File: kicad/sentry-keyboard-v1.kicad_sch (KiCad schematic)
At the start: 269 parts, among them J2 Conn_01x04, J4 AVR-ISP-6, SW1 Reset, SW2 RotaryEncoder_Switch, U1 ATmega32U4-AU, Y1 16Mhz

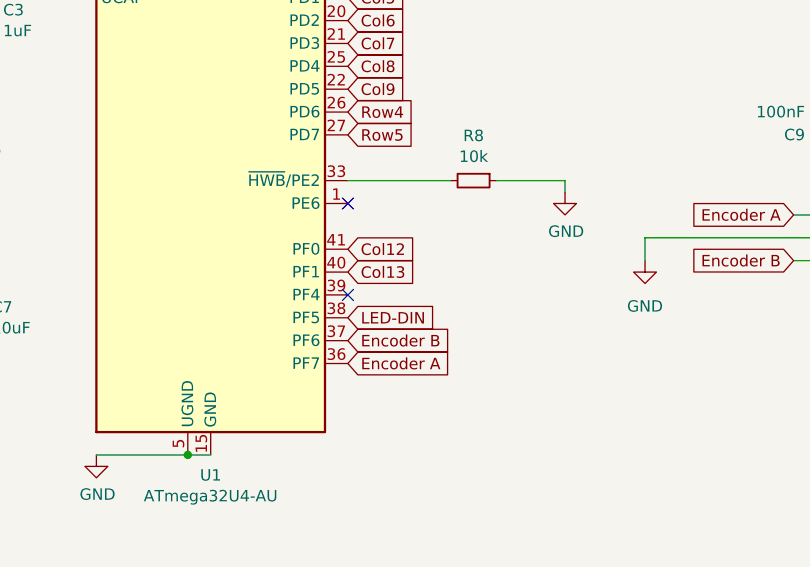
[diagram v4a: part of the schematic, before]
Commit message: Route col 12 and 13
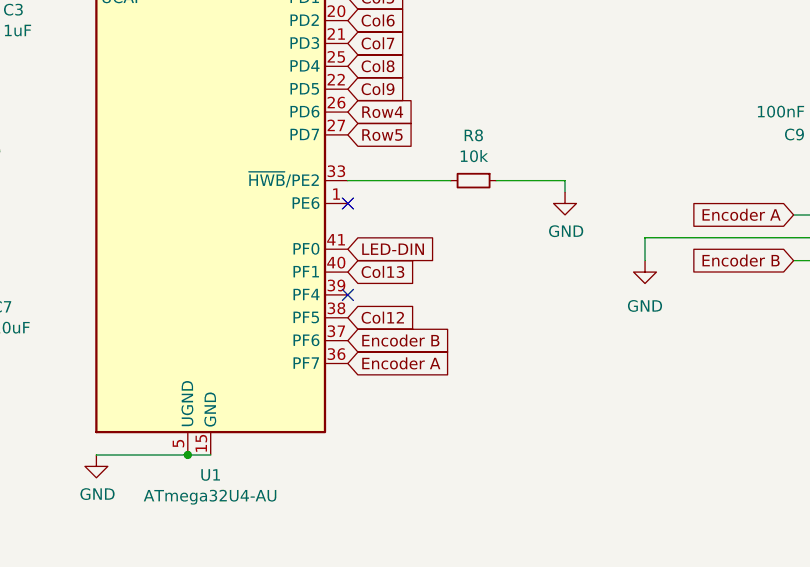
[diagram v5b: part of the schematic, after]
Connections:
- net Col12: now also U1.38 (PF5); no longer U1.41 (PF0)
- net LED-DIN: now also U1.41 (PF0); no longer U1.38 (PF5)
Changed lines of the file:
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@@
+		)
+	)
+	(global_label "LED-DIN"
+		(shape input)
+		(at 96.52 110.49 0)
+		(fields_autoplaced yes)
+		(effects
+			(font
+				(size 1.27 1.27)
+			)
+			(justify left)
+		)
+		(property "Intersheetrefs" "${INTERSHEET_REFS}"
+			(at 107.73 110.49 0)
+			(effects
+				(font
+					(size 1.27 1.27)
+				)
+				(justify left)
+				(hide yes)
+			)
 		)
 	)
@@
 		)
 	)
+	(global_label "Col12"
+		(shape input)
+		(at 96.52 118.11 0)
+		(fields_autoplaced yes)
+		(effects
+			(font
+				(size 1.27 1.27)
+			)
+			(justify left)
+		)
+		(property "Intersheetrefs" "${INTERSHEET_REFS}"
+			(at 105.0084 118.11 0)
+			(effects
+				(font
+					(size 1.27 1.27)
+				)
+				(justify left)
+				(hide yes)
+			)
+		)
+	)
 	(global_label "Col1"
 		(shape input)
@@
 		)
 	)
-	(global_label "LED-DIN"
-		(shape input)
-		(at 96.52 118.11 0)
-		(fields_autoplaced yes)
-		(effects
-			(font
-				(size 1.27 1.27)
-			)
-			(justify left)
-		)
-		(property "Intersheetrefs" "${INTERSHEET_REFS}"
-			(at 107.73 118.11 0)
-			(effects
-				(font
-					(size 1.27 1.27)
-				)
-				(justify left)
-				(hide yes)
-			)
-		)
-	)
 	(global_label "Row5"
 		(shape input)
@@
 			(effects
 				(font
-					(size 1.27 1.27)
-				)
-				(justify left)
-				(hide yes)
-			)
-		)
-	)
-	(global_label "Col12"
-		(shape input)
-		(at 96.52 110.49 0)
-		(fields_autoplaced yes)
-		(effects
-			(font
-				(size 1.27 1.27)
-			)
-			(justify left)
-		)
-		(property "Intersheetrefs" "${INTERSHEET_REFS}"
-			(at 105.0084 110.49 0)
-			(effects
-				(font

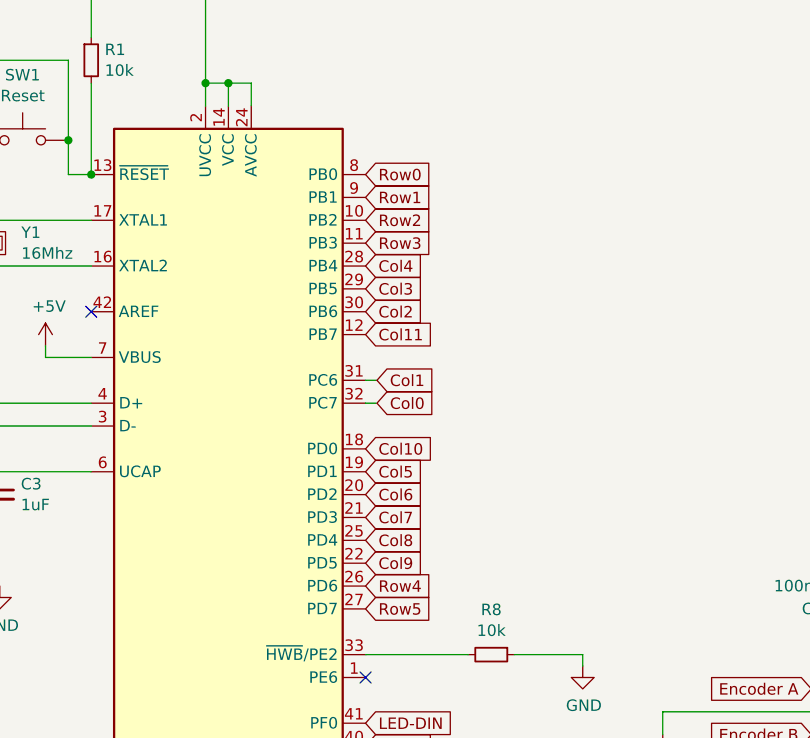
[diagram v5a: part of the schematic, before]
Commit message: route more of the switch matrix
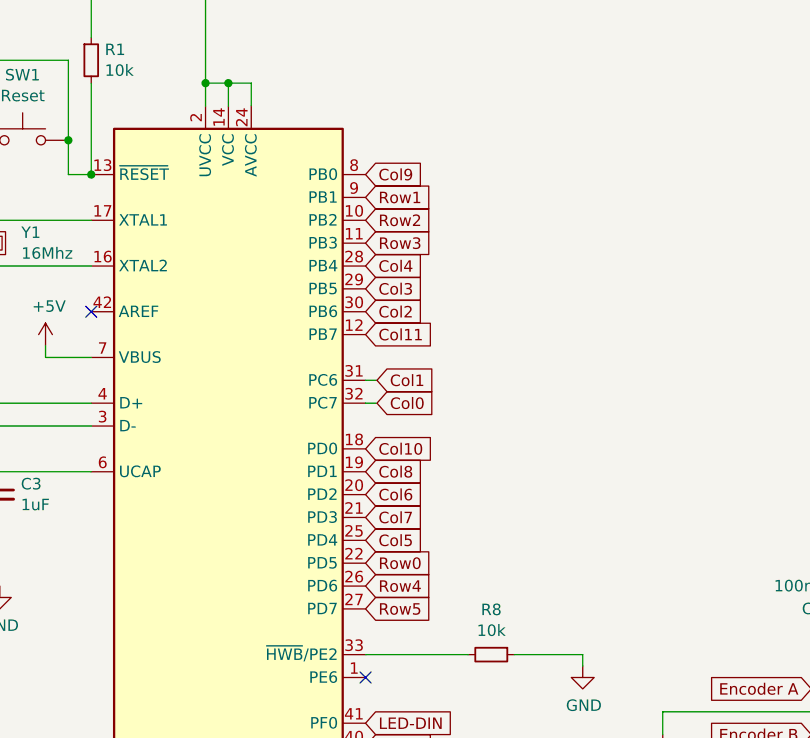
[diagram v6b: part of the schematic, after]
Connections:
- net Col5: now also U1.25 (PD4); no longer U1.19 (PD1)
- net Col8: now also U1.19 (PD1); no longer U1.25 (PD4)
- net Col9: now also U1.8 (PB0); no longer U1.22 (PD5)
- net Row0: now also U1.22 (PD5); no longer U1.8 (PB0)

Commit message: Rough routing is complete
Still lots of small tweaks and clean up to do.
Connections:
- net Col6: now also U1.11 (PB3); no longer U1.20 (PD2)
- net Col7: now also U1.10 (PB2); no longer U1.21 (PD3)
- net Col8: now also U1.9 (PB1); no longer U1.19 (PD1)
- net Row1: now also U1.20 (PD2); no longer U1.9 (PB1)
- net Row2: now also U1.21 (PD3); no longer U1.10 (PB2)
- net Row3: now also U1.19 (PD1); no longer U1.11 (PB3)

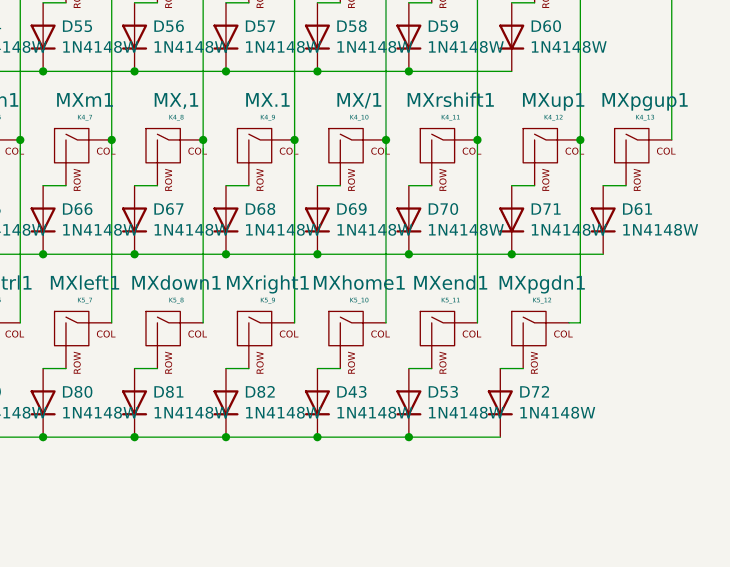
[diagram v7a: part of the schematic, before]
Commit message: Fix ordering of home/end
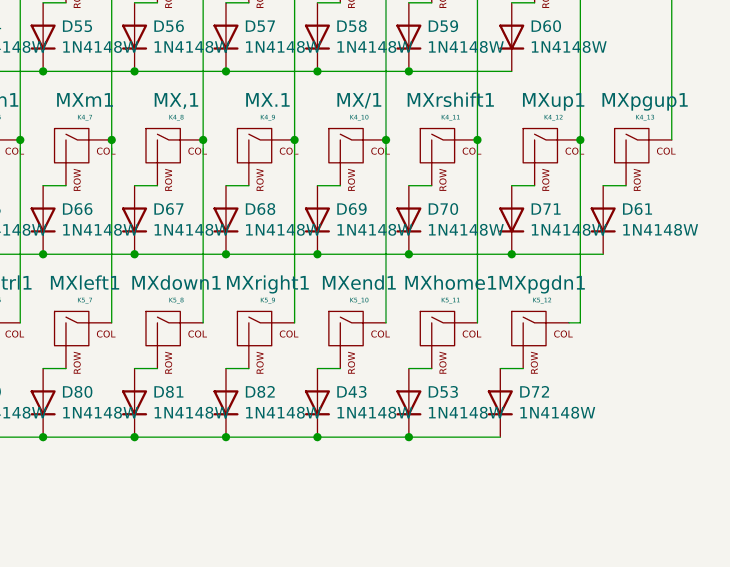
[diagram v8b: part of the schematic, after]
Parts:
- renumbered MXhome1 to MXend1, MXend1 to MXhome1
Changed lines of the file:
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@@
 		(on_board yes)
 		(dnp no)
-		(property "Reference" "MXhome1"
+		(property "Reference" "MXend1"
 			(at 347.5482 131.4958 0)
 			(effects
@@
 			(project "sentry-keyboard-v1"
 				(path "/db914c1a-35d4-4b87-a1dd-e01e7dff4eef"
-					(reference "MXhome1")
+					(reference "MXend1")
 					(unit 1)
 				)
@@
 		(on_board yes)
 		(dnp no)
-		(property "Reference" "MXend1"
+		(property "Reference" "MXhome1"
 			(at 357.7082 131.4958 0)
 			(effects
@@
 			(project "sentry-keyboard-v1"
 				(path "/db914c1a-35d4-4b87-a1dd-e01e7dff4eef"
-					(reference "MXend1")
-					(unit 1)
-				)
+					(reference "MXhome1")
+					(unit 1)
+				)
